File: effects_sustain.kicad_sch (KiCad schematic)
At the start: 13 parts, among them Q1 Q_NPN_BCE

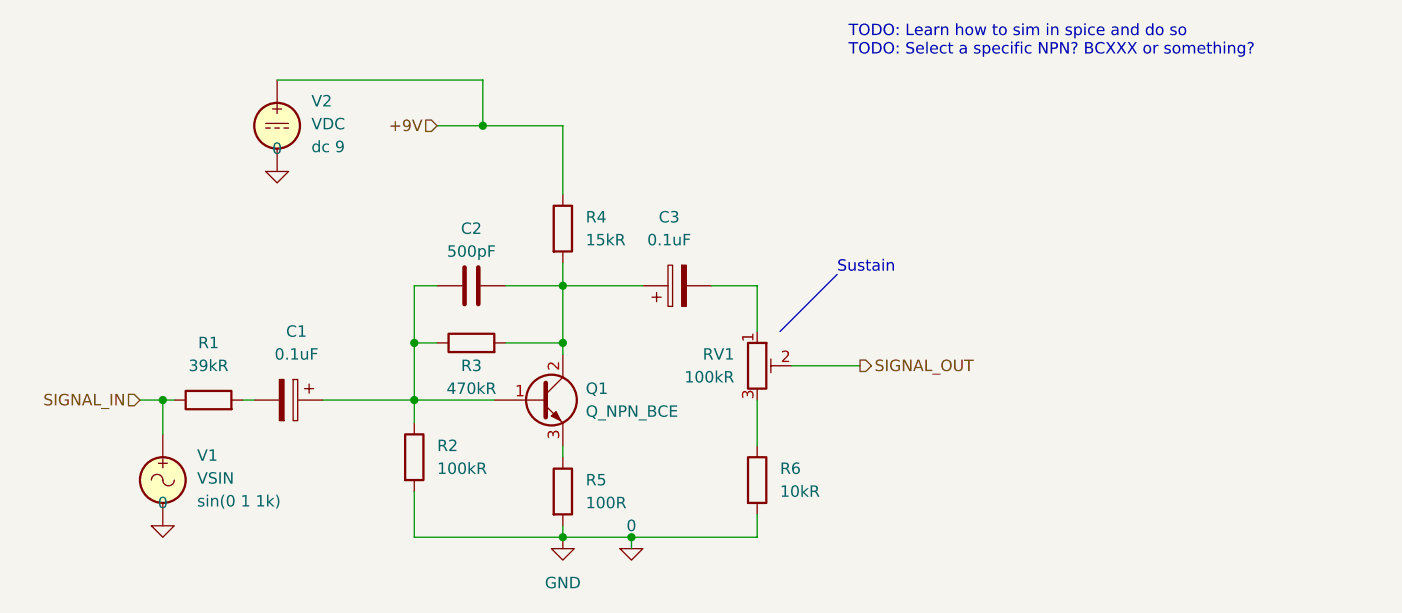
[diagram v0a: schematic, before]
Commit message: added README, added design notes, simulated sustain circuit by making a copy as a new project, separated all spice elements from the original schematic, added a sim model library
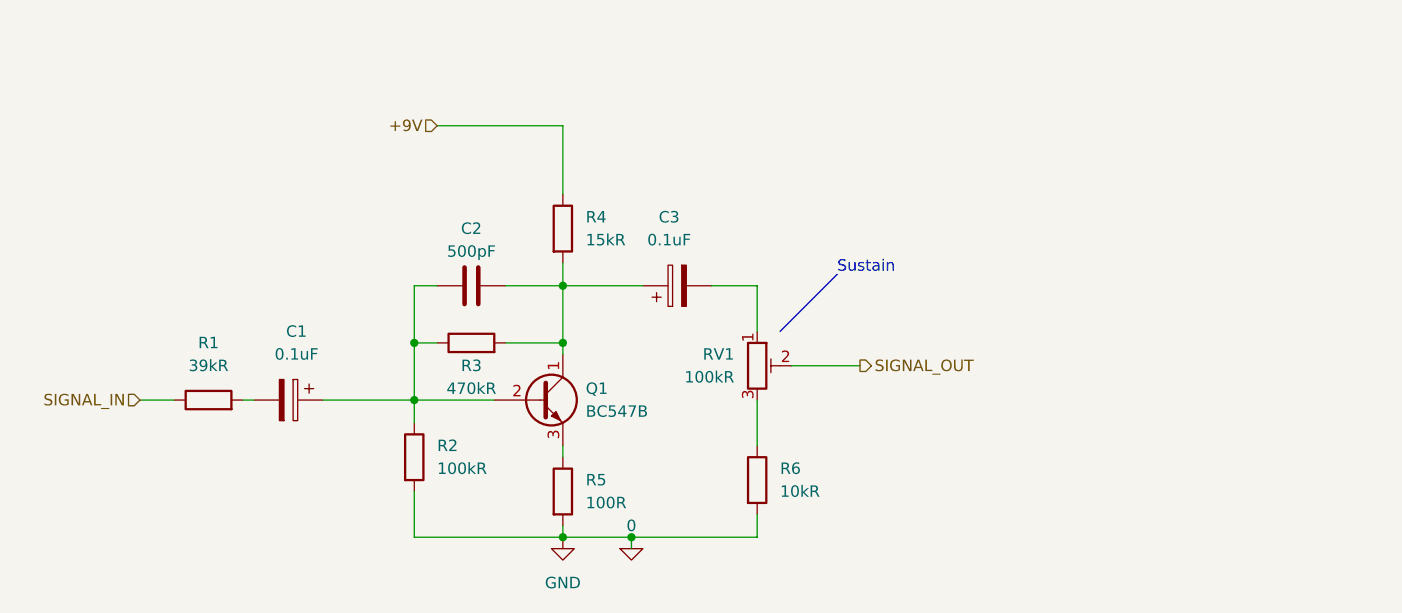
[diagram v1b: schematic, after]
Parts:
- removed Q1: Q_NPN_BCE, symbol Device:Q_NPN_BCE
- removed V1: VSIN, symbol Simulation_SPICE:VSIN
- removed V2: VDC, symbol Simulation_SPICE:VDC
- added Q1: BC547B, Package_TO_SOT_THT:TO-92_Inline, symbol Transistor_BJT:BC547
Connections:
- net at R5.1: now also Q1.3 (E)
- net at C1.1, C2.1, R2.1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: now also Q1.2 (B)
- net at C2.2, C3.1, R3.2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: now also Q1.1 (C)
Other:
- note removed: "TODO: Learn how to sim in spice and do so TODO: Select a specific NPN? BCXXX or something?"
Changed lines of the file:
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@@
   (junction (at 113.03 105.41) (diameter 0) (color 0 0 0 0)
   )
-  (junction (at 68.58 90.17) (diameter 0) (color 0 0 0 0)
-  )
-  (junction (at 104.14 59.69) (diameter 0) (color 0 0 0 0)
-  )
   (junction (at 96.52 90.17) (diameter 0) (color 0 0 0 0)
   )
@@
     (stroke (width 0) (type default) (color 0 0 0 0))
   )
-  (wire (pts (xy 68.58 90.17) (xy 68.58 93.98))
-    (stroke (width 0) (type default) (color 0 0 0 0))
-  )
   (wire (pts (xy 134.62 105.41) (xy 120.65 105.41))
     (stroke (width 0) (type default) (color 0 0 0 0))
@@
     (stroke (width 0) (type default) (color 0 0 0 0))
   )
-  (wire (pts (xy 68.58 90.17) (xy 69.85 90.17))
+  (wire (pts (xy 66.04 90.17) (xy 69.85 90.17))
     (stroke (width 0) (type default) (color 0 0 0 0))
   )
@@
     (stroke (width 0) (type default) (color 0 0 0 0))
   )
-  (wire (pts (xy 104.14 54.61) (xy 104.14 59.69))
-    (stroke (width 0) (type default) (color 0 0 0 0))
-  )
   (wire (pts (xy 113.03 95.25) (xy 113.03 96.52))
     (stroke (width 0) (type default) (color 0 0 0 0))
   )
-  (wire (pts (xy 81.28 54.61) (xy 104.14 54.61))
-    (stroke (width 0) (type default) (color 0 0 0 0))
-  )
   (wire (pts (xy 96.52 105.41) (xy 113.03 105.41))
     (stroke (width 0) (type default) (color 0 0 0 0))
@@
     (stroke (width 0) (type default) (color 0 0 0 0))
   )
-  (wire (pts (xy 104.14 59.69) (xy 99.06 59.69))
-    (stroke (width 0) (type default) (color 0 0 0 0))
-  )
-  (wire (pts (xy 66.04 90.17) (xy 68.58 90.17))
+  (wire (pts (xy 99.06 59.69) (xy 113.03 59.69))
     (stroke (width 0) (type default) (color 0 0 0 0))
   )
@@
   )
   (wire (pts (xy 96.52 77.47) (xy 96.52 83.82))
-    (stroke (width 0) (type default) (color 0 0 0 0))
-  )
-  (wire (pts (xy 113.03 59.69) (xy 104.14 59.69))
     (stroke (width 0) (type default) (color 0 0 0 0))
   )
@@
     (stroke (width 0) (type default) (color 0 0 0 0))
   )
-  (text "TODO: Learn how to sim in spice and do so\nTODO: Select a specific NPN? BCXXX or something?"
-    (at 144.78 52.07 0)
-    (effects (font (size 1.27 1.27)) (justify left bottom))
-  )
   (text "Sustain" (at 143.51 76.2 0)
     (effects (font (size 1.27 1.27)) (justify left bottom))
@@
     (pin "1")
     (pin "2")
-  )
-  (symbol (lib_id "pspice:0") (at 68.58 104.14 0) (unit 1)
-    (in_bom yes) (on_board yes) (fields_autoplaced)
-    (property "Reference" "#GND01" (id 0) (at 68.58 106.68 0)
-      (effects (font (size 1.27 1.27)) hide)
-    )
-    (property "Value" "0" (id 1) (at 68.58 101.6 0))
-    (property "Footprint" "" (id 2) (at 68.58 104.14 0)
-      (effects (font (size 1.27 1.27)) hide)
-    )
-    (property "Datasheet" "~" (id 3) (at 68.58 104.14 0)
-      (effects (font (size 1.27 1.27)) hide)
-    )
-    (pin "1")
   )
   (symbol (lib_id "Device:R") (at 102.87 83.82 90) (unit 1)
@@
     (pin "2")
   )
-  (symbol (lib_id "Simulation_SPICE:VSIN") (at 68.58 99.06 0) (unit 1)
-    (in_bom yes) (on_board yes) (fields_autoplaced)
-    (property "Reference" "V1" (id 0) (at 72.39 96.3301 0)
-      (effects (font (size 1.27 1.27)) (justify left))
-    )
-    (property "Value" "VSIN" (id 1) (at 72.39 98.8701 0)
-      (effects (font (size 1.27 1.27)) (justify left))
-    )
-    (property "Footprint" "" (id 2) (at 68.58 99.06 0)
-      (effects (font (size 1.27 1.27)) hide)
-    )
-    (property "Datasheet" "~" (id 3) (at 68.58 99.06 0)
-      (effects (font (size 1.27 1.27)) hide)
-    )
-    (property "Spice_Netlist_Enabled" "Y" (id 4) (at 68.58 99.06 0)
-      (effects (font (size 1.27 1.27)) (justify left) hide)
-    )
-    (property "Spice_Primitive" "V" (id 5) (at 68.58 99.06 0)
-      (effects (font (size 1.27 1.27)) (justify left) hide)
-    )
-    (property "Spice_Model" "sin(0 1 1k)" (id 6) (at 72.39 101.4101 0)
-      (effects (font (size 1.27 1.27)) (justify left))
-    )
-    (pin "1")
-    (pin "2")
-  )
-  (symbol (lib_id "Simulation_SPICE:VDC") (at 81.28 59.69 0) (unit 1)
-    (in_bom yes) (on_board yes) (fields_autoplaced)
-    (property "Reference" "V2" (id 0) (at 85.09 56.9601 0)
-      (effects (font (size 1.27 1.27)) (justify left))
-    )
-    (property "Value" "VDC" (id 1) (at 85.09 59.5001 0)
-      (effects (font (size 1.27 1.27)) (justify left))
-    )
-    (property "Footprint" "" (id 2) (at 81.28 59.69 0)
-      (effects (font (size 1.27 1.27)) hide)
-    )
-    (property "Datasheet" "~" (id 3) (at 81.28 59.69 0)
-      (effects (font (size 1.27 1.27)) hide)
-    )
-    (property "Spice_Netlist_Enabled" "Y" (id 4) (at 81.28 59.69 0)
-      (effects (font (size 1.27 1.27)) (justify left) hide)
-    )
-    (property "Spice_Primitive" "V" (id 5) (at 81.28 59.69 0)
-      (effects (font (size 1.27 1.27)) (justify left) hide)
-    )
-    (property "Spice_Model" "dc 9" (id 6) (at 85.09 62.0401 0)
-      (effects (font (size 1.27 1.27)) (justify left))
-    )
-    (pin "1")
-    (pin "2")
-  )
-  (symbol (lib_id "pspice:0") (at 81.28 64.77 0) (unit 1)
-    (in_bom yes) (on_board yes) (fields_autoplaced)
-    (property "Reference" "#GND02" (id 0) (at 81.28 67.31 0)
-      (effects (font (size 1.27 1.27)) hide)
-    )
-    (property "Value" "0" (id 1) (at 81.28 62.23 0))
-    (property "Footprint" "" (id 2) (at 81.28 64.77 0)
-      (effects (font (size 1.27 1.27)) hide)
-    )
-    (property "Datasheet" "~" (id 3) (at 81.28 64.77 0)
-      (effects (font (size 1.27 1.27)) hide)
-    )
-    (pin "1")
-  )
   (symbol (lib_id "Device:C_Polarized") (at 82.55 90.17 270) (unit 1)
     (in_bom yes) (on_board yes) (fields_autoplaced)
@@
     (pin "1")
     (pin "2")
+  )
+  (symbol (lib_id "Transistor_BJT:BC547") (at 110.49 90.17 0) (unit 1)
+    (in_bom yes) (on_board yes) (fields_autoplaced)
+    (property "Reference" "Q1" (id 0) (at 115.57 88.8999 0)
+      (effects (font (size 1.27 1.27)) (justify left))
+    )
+    (property "Value" "BC547B" (id 1) (at 115.57 91.4399 0)
+      (effects (font (size 1.27 1.27)) (justify left))
+    )
+    (property "Footprint" "Package_TO_SOT_THT:TO-92_Inline" (id 2) (at 115.57 92.075 0)
+      (effects (font (size 1.27 1.27) italic) (justify left) hide)
+    )
+    (property "Datasheet" "https://www.onsemi.com/pub/Collateral/BC550-D.pdf" (id 3) (at 110.49 90.17 0)
+      (effects (font (size 1.27 1.27)) (justify left) hide)
+    )
+    (pin "1")
+    (pin "2")
+    (pin "3")
   )
   (symbol (lib_id "Device:C") (at 102.87 77.47 90) (unit 1)
@@
     (pin "2")
   )
-  (symbol (lib_id "Device:Q_NPN_BCE") (at 110.49 90.17 0) (unit 1)
-    (in_bom yes) (on_board yes) (fields_autoplaced)
-    (property "Reference" "Q1" (id 0) (at 115.57 88.8999 0)
-      (effects (font (size 1.27 1.27)) (justify left))
-    )
-    (property "Value" "Q_NPN_BCE" (id 1) (at 115.57 91.4399 0)
-      (effects (font (size 1.27 1.27)) (justify left))
-    )
-    (property "Footprint" "" (id 2) (at 115.57 87.63 0)
-      (effects (font (size 1.27 1.27)) hide)
-    )
-    (property "Datasheet" "~" (id 3) (at 110.49 90.17 0)
-      (effects (font (size 1.27 1.27)) hide)
-    )
-    (property "Spice_Primitive" "Q" (id 4) (at 110.49 90.17 0)
-      (effects (font (size 1.27 1.27)) hide)
-    )
-    (property "Spice_Model" "Q_NPN_BCE" (id 5) (at 110.49 90.17 0)
-      (effects (font (size 1.27 1.27)) hide)
-    )
-    (property "Spice_Netlist_Enabled" "Y" (id 6) (at 110.49 90.17 0)
-      (effects (font (size 1.27 1.27)) hide)
-    )
-    (pin "1")
-    (pin "2")
-    (pin "3")
-  )
 )

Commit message: added decoupling cap and series resistor to output side of sustain effect, added subfolder to contain simulation results to put in design notes. Added simulation results for sustain effect to design notes
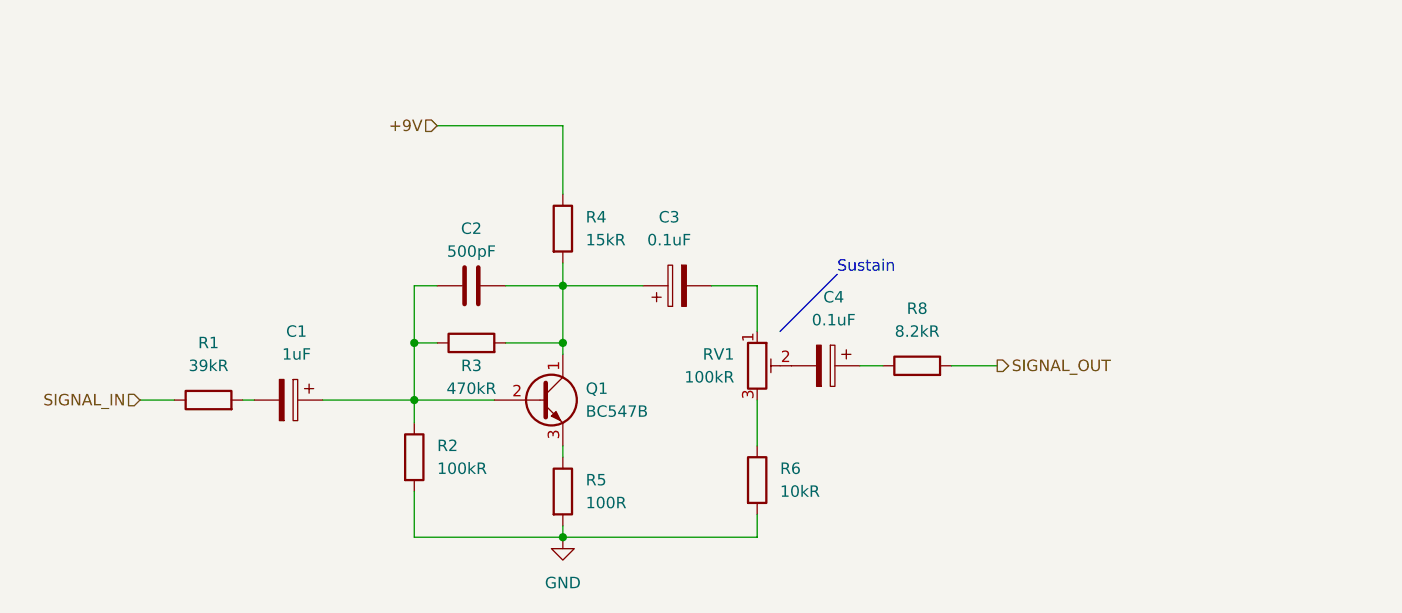
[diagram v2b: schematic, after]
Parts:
- added C4: 0.1uF, symbol Device:C_Polarized
- added R8: 8.2kR, symbol Device:R
- C1: value 0.1uF -> 1uF
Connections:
- net SIGNAL_OUT: now also R8.2; no longer RV1.2
- net 0 renamed GND
- new net: C4.2, RV1.2
- new net: C4.1, R8.1
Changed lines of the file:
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@@
     (rev "V0.1")
   )
-  (junction (at 120.65 105.41) (diameter 0) (color 0 0 0 0)
-  )
   (junction (at 96.52 83.82) (diameter 0) (color 0 0 0 0)
   )
@@
     (stroke (width 0) (type default) (color 0 0 0 0))
   )
-  (wire (pts (xy 134.62 105.41) (xy 120.65 105.41))
+  (wire (pts (xy 113.03 105.41) (xy 134.62 105.41))
     (stroke (width 0) (type default) (color 0 0 0 0))
   )
@@
     (stroke (width 0) (type default) (color 0 0 0 0))
   )
-  (wire (pts (xy 138.43 86.36) (xy 146.05 86.36))
-    (stroke (width 0) (type default) (color 0 0 0 0))
-  )
   (wire (pts (xy 96.52 90.17) (xy 96.52 92.71))
     (stroke (width 0) (type default) (color 0 0 0 0))
@@
     (stroke (width 0) (type default) (color 0 0 0 0))
   )
-  (wire (pts (xy 120.65 105.41) (xy 120.65 106.68))
-    (stroke (width 0) (type default) (color 0 0 0 0))
-  )
   (wire (pts (xy 78.74 90.17) (xy 77.47 90.17))
     (stroke (width 0) (type default) (color 0 0 0 0))
@@
     (stroke (width 0) (type default) (color 0 0 0 0))
   )
+  (wire (pts (xy 146.05 86.36) (xy 148.59 86.36))
+    (stroke (width 0) (type default) (color 0 0 0 0))
+  )
   (wire (pts (xy 96.52 83.82) (xy 99.06 83.82))
+    (stroke (width 0) (type default) (color 0 0 0 0))
+  )
+  (wire (pts (xy 156.21 86.36) (xy 161.29 86.36))
     (stroke (width 0) (type default) (color 0 0 0 0))
   )
@@
     (stroke (width 0) (type default) (color 0 0 0 0))
   )
-  (wire (pts (xy 120.65 105.41) (xy 113.03 105.41))
-    (stroke (width 0) (type default) (color 0 0 0 0))
-  )
   (wire (pts (xy 96.52 90.17) (xy 105.41 90.17))
     (stroke (width 0) (type default) (color 0 0 0 0))
@@
     (effects (font (size 1.27 1.27)) (justify right))
   )
-  (hierarchical_label "SIGNAL_OUT" (shape output) (at 146.05 86.36 0)
+  (hierarchical_label "SIGNAL_OUT" (shape output) (at 161.29 86.36 0)
     (effects (font (size 1.27 1.27)) (justify left))
   )
@@
     )
     (property "Datasheet" "~" (id 3) (at 134.62 99.06 0)
+      (effects (font (size 1.27 1.27)) hide)
+    )
+    (pin "1")
+    (pin "2")
+  )
+  (symbol (lib_id "Device:C_Polarized") (at 142.24 86.36 270) (unit 1)
+    (in_bom yes) (on_board yes) (fields_autoplaced)
+    (property "Reference" "C4" (id 0) (at 143.129 78.74 90))
+    (property "Value" "0.1uF" (id 1) (at 143.129 81.28 90))
+    (property "Footprint" "" (id 2) (at 138.43 87.3252 0)
+      (effects (font (size 1.27 1.27)) hide)
+    )
+    (property "Datasheet" "~" (id 3) (at 142.24 86.36 0)
       (effects (font (size 1.27 1.27)) hide)
     )
@@
     (pin "2")
   )
-  (symbol (lib_id "pspice:0") (at 120.65 106.68 0) (unit 1)
-    (in_bom yes) (on_board yes) (fields_autoplaced)
-    (property "Reference" "#GND03" (id 0) (at 120.65 109.22 0)
-      (effects (font (size 1.27 1.27)) hide)
-    )
-    (property "Value" "0" (id 1) (at 120.65 104.14 0))
-    (property "Footprint" "" (id 2) (at 120.65 106.68 0)
-      (effects (font (size 1.27 1.27)) hide)
-    )
-    (property "Datasheet" "~" (id 3) (at 120.65 106.68 0)
-      (effects (font (size 1.27 1.27)) hide)
-    )
-    (pin "1")
-  )
   (symbol (lib_id "power:GND") (at 113.03 105.41 0) (unit 1)
     (in_bom yes) (on_board yes) (fields_autoplaced)
@@
     (pin "2")
   )
+  (symbol (lib_id "Device:R") (at 152.4 86.36 90) (unit 1)
+    (in_bom yes) (on_board yes) (fields_autoplaced)
+    (property "Reference" "R8" (id 0) (at 152.4 80.01 90))
+    (property "Value" "8.2kR" (id 1) (at 152.4 82.55 90))
+    (property "Footprint" "" (id 2) (at 152.4 88.138 90)
+      (effects (font (size 1.27 1.27)) hide)
+    )
+    (property "Datasheet" "~" (id 3) (at 152.4 86.36 0)
+      (effects (font (size 1.27 1.27)) hide)
+    )
+    (pin "1")
+    (pin "2")
+  )
   (symbol (lib_id "Device:C_Polarized") (at 82.55 90.17 270) (unit 1)
     (in_bom yes) (on_board yes) (fields_autoplaced)
     (property "Reference" "C1" (id 0) (at 83.439 82.55 90))
-    (property "Value" "0.1uF" (id 1) (at 83.439 85.09 90))
+    (property "Value" "1uF" (id 1) (at 83.439 85.09 90))
     (property "Footprint" "" (id 2) (at 78.74 91.1352 0)
       (effects (font (size 1.27 1.27)) hide)
